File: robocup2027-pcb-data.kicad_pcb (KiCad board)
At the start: 2 copper layers, 36 parts, among them M5 Motor_Servo, M6 Motor_Servo, Q1 BPW40, Q2 BPW40, U1 ESP32-DEVKITC-32E

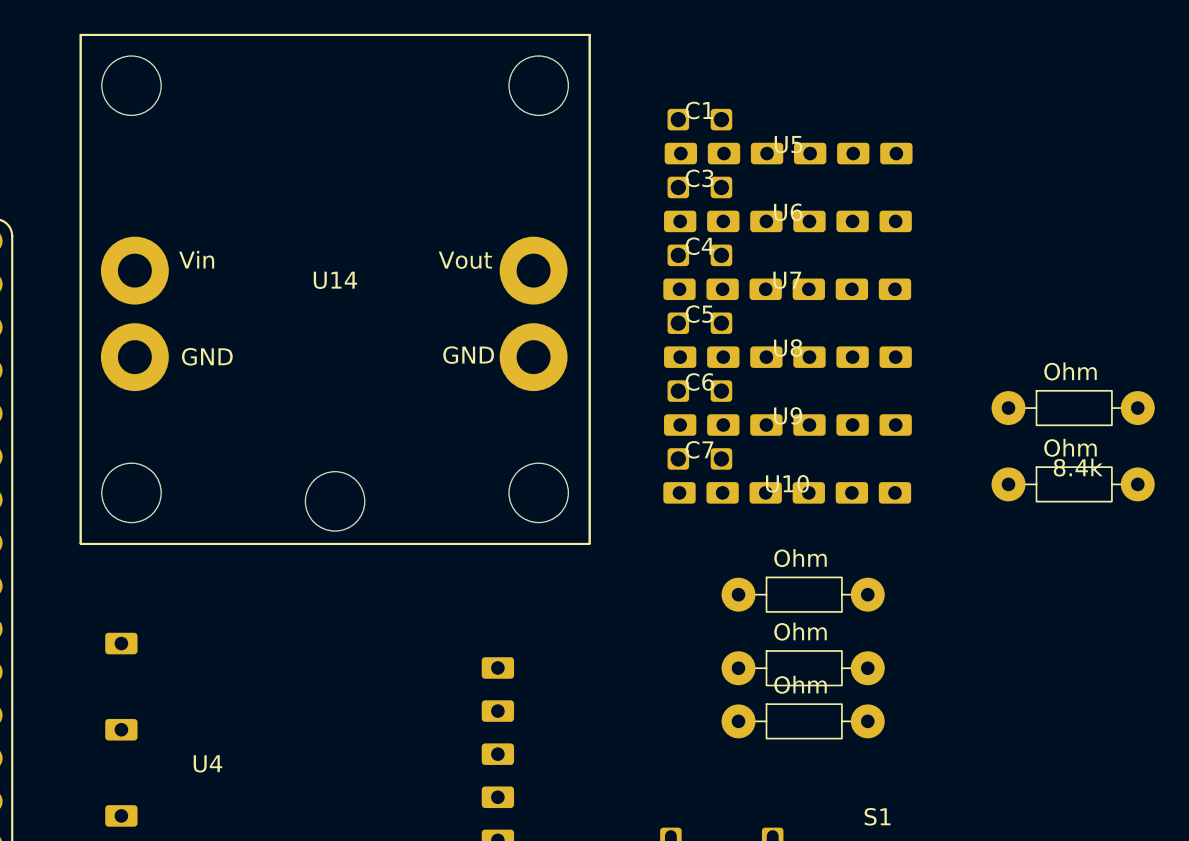
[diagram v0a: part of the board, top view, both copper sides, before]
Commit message: fixed footprint
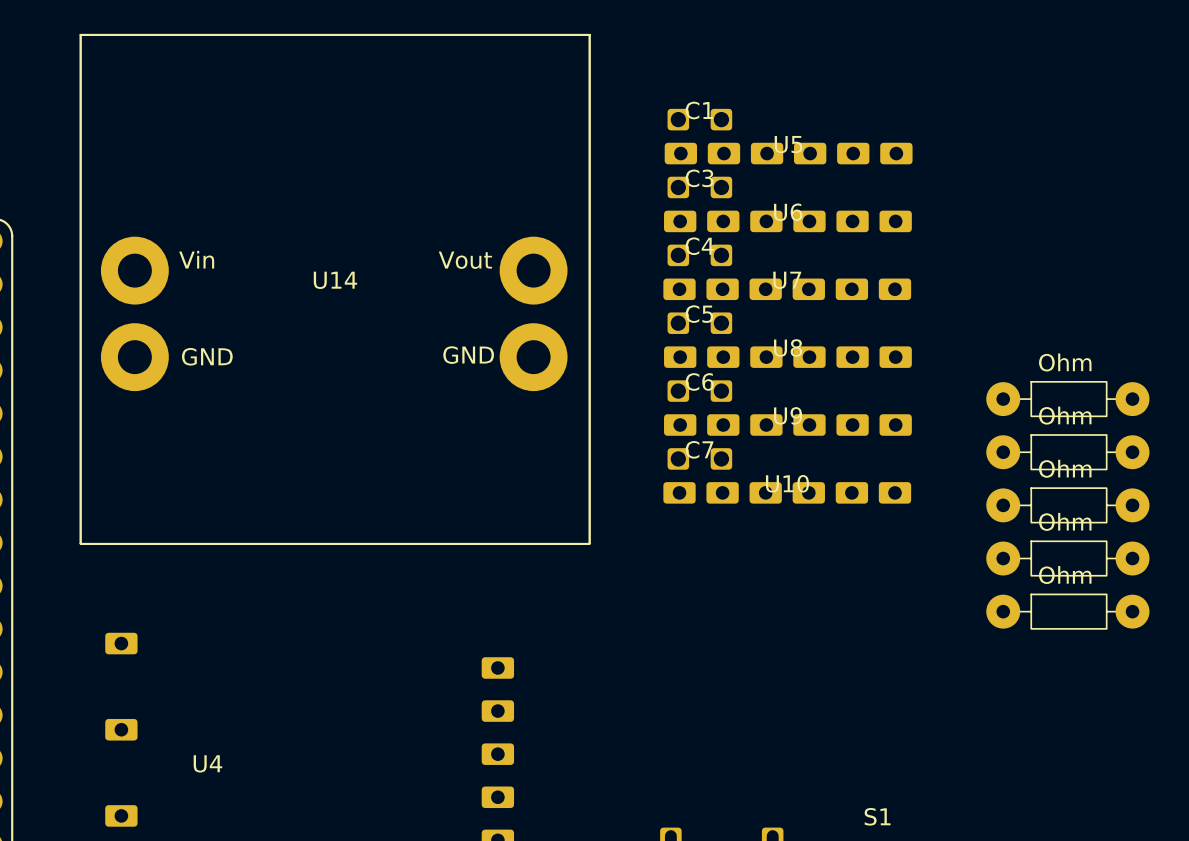
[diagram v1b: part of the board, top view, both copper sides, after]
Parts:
- moved R4 16.9 mm to (184.2, 69.4)
- moved R5 16.9 mm to (184.2, 72.5)
- moved R3 16.5 mm to (184.2, 66.2)
- moved R2 1.92 mm to (184.2, 63.1)
- moved R1 0.61 mm to (184.2, 60.0)

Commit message: update
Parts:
- C2, C8: footprint robo:5.08mm_capacitor_1 -> robo:capacitor
- Q1, Q2: footprint LED_THT:LED_D5.0mm_Clear -> robo:2.54mm_capacitor
- U11: footprint robo:M78AR033 -> robo:DCDC-M78AR033-0.5
- moved D2 29.7 mm to (104.4, 122.2)
- moved D1 29.1 mm to (105.2, 115.9)
- moved C8 27.8 mm to (123.1, 115.4)
- moved U11 25.6 mm to (124.5, 125.3)
- moved Q1 17.0 mm to (98.2, 114.9)
- moved Q2 17.0 mm to (98.4, 123.9)
- moved C2 2.43 mm to (151.4, 116.3)

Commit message: placed stuff
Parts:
- added C9: 0.1uF, robo:2.54mm_capacitor, F.Cu at (54.2, 72.5)
- added M1: ~, robo:sts3032, F.Cu at (68.5, 63.9)
- added M2: ~, robo:sts3032, F.Cu at (68.5, 66.2)
- added M3: ~, robo:sts3032, F.Cu at (68.5, 68.4)
- added M4: ~, robo:sts3032, F.Cu at (68.5, 70.7)
- added M7: ~, robo:sts3032, F.Cu at (68.5, 73.0)
- added M8: ~, robo:sts3032, F.Cu at (68.5, 75.2)
- added M9: ~, robo:sts3032, F.Cu at (68.5, 77.5)
- added U13: ~, robo:fe-urt-2, F.Cu at (58.4, 61.6)
- added U15: ~, robo:VL53L1X-ToF, F.Cu at (59.6, 59.3)
- added U16: ~, robo:DCDC-M78AR033-0.5, F.Cu at (58.1, 65.3)
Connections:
- U1 pad J3_11: unconnected-(U1-IO17-PadJ3_11) -> FE-URT-2-TXD
- U1 pad J3_12: unconnected-(U1-IO16-PadJ3_12) -> FE-URT-2-RXD

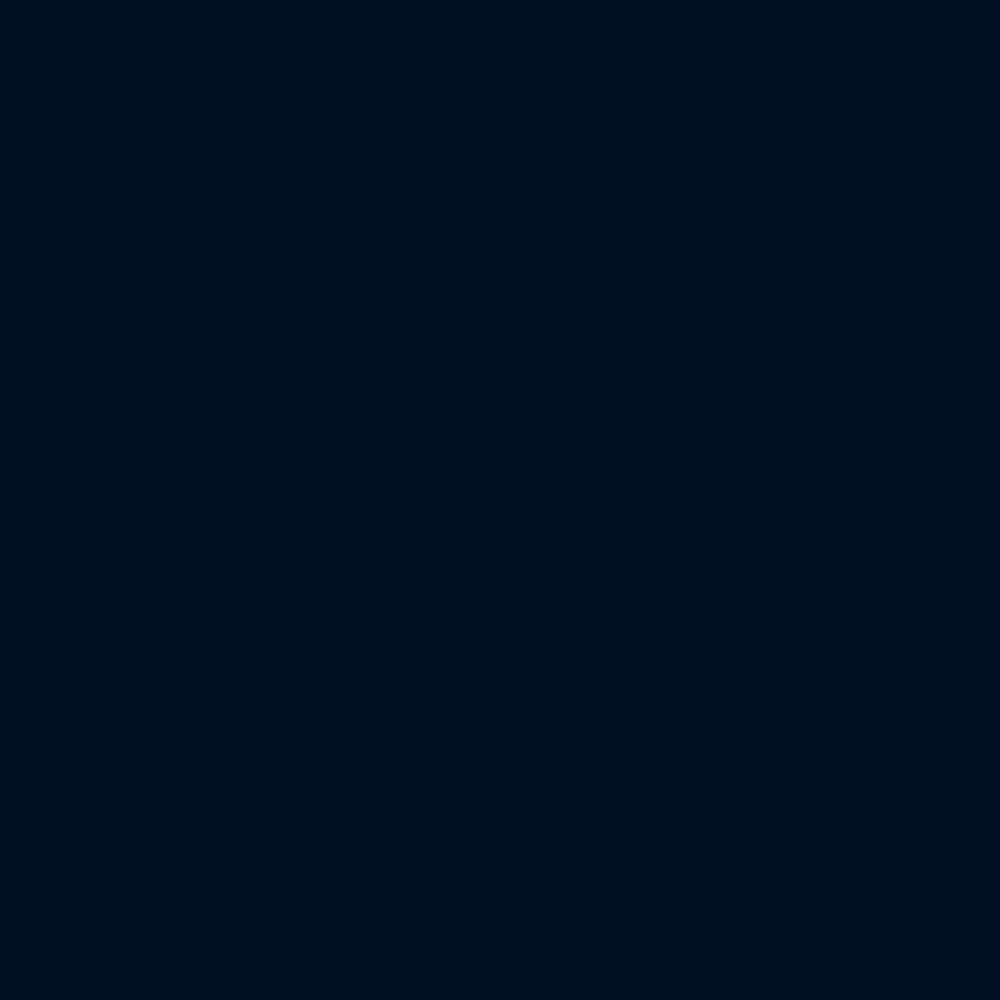
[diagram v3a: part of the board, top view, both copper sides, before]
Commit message: assigned footprints and added them to pcb
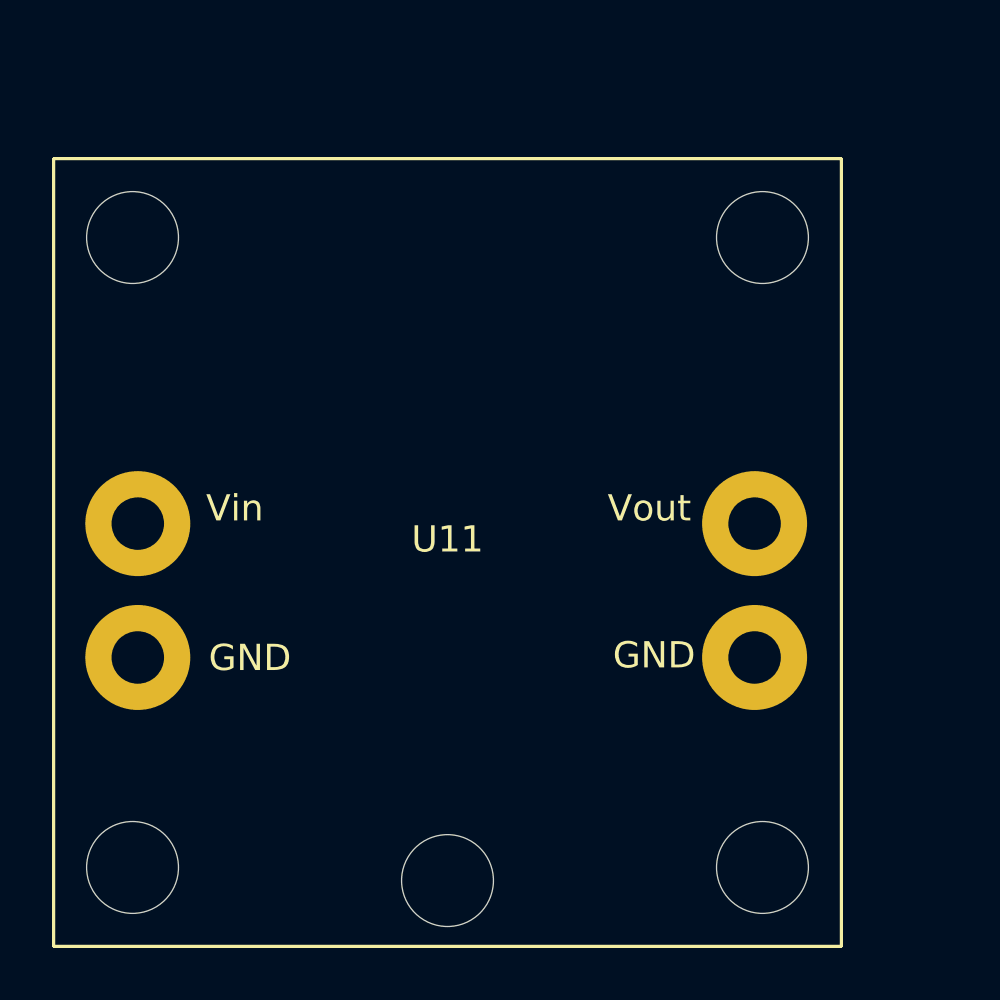
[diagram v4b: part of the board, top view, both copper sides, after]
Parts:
- added U11: ~, robo:DCDC-LTC3111, F.Cu at (57.0, 121.5)
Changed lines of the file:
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@@
+		(embedded_fonts no)
+	)
+	(footprint "robo:DCDC-LTC3111"
+		(layer "F.Cu")
+		(at 57 121.5)
+		(property "Reference" "U11"
+			(at 0 -0.5 0)
+			(unlocked yes)
+			(layer "F.SilkS")
+			(effects
+				(font
+					(size 1 1)
+					(thickness 0.1)
+				)
+			)
+		)
+		(property "Value" "~"
+			(at 0 1 0)
+			(unlocked yes)
+			(layer "F.Fab")
+			(effects
+				(font
+					(size 1 1)
+					(thickness 0.15)
+				)
+			)
+		)
+		(property "Datasheet" ""
+			(at 0 0 0)
+			(unlocked yes)
+			(layer "F.Fab")
+			(hide yes)
+			(effects
+				(font
+					(size 1 1)
+					(thickness 0.15)
+				)
+			)
+		)
+		(property "Description" ""
+			(at 0 0 0)
+			(unlocked yes)
+			(layer "F.Fab")
+			(hide yes)
+			(effects
+				(font
+					(size 1 1)
+					(thickness 0.15)
+				)
+			)
+		)
+		(sheetname "/")
+		(sheetfile "robocup2027-pcb-data.kicad_sch")
+		(attr through_hole)
+		(fp_rect
+			(start -15 -15)
+			(end -15 15)
+			(stroke
+				(width 0.1)
+				(type default)
+			)
+			(fill no)
+			(layer "F.SilkS")
+		)
+		(fp_rect
+			(start -15 -15)
+			(end 15 -15)
+			(stroke
+				(width 0.1)
+				(type default)
+			)
+			(fill no)
+			(layer "F.SilkS")
+		)
+		(fp_rect
+			(start -15 15)
+			(end 15 15)
+			(stroke
+				(width 0.1)
+				(type default)
+			)
+			(fill no)
+			(layer "F.SilkS")
+		)
+		(fp_rect
+			(start 15 -15)
+			(end 15 15)
+			(stroke
+				(width 0.1)
+				(type default)
+			)
+			(fill no)
+			(layer "F.SilkS")
+		)
+		(fp_text user "Vin"
+			(at -9.2 -1.1 0)
+			(unlocked yes)
+			(layer "F.SilkS")
+			(effects
+				(font
+					(size 1 1)
+					(thickness 0.1)
+				)
+				(justify left bottom)
+			)
+		)
+		(fp_text user "GND"
+			(at -9.1 4.6 0)
+			(unlocked yes)
+			(layer "F.SilkS")
+			(effects
+				(font
+					(size 1 1)
+					(thickness 0.1)
+				)
+				(justify left bottom)
+			)
+		)
+		(fp_text user "Vout"
+			(at 6.1 -1.1 0)
+			(unlocked yes)
+			(layer "F.SilkS")
+			(effects
+				(font
+					(size 1 1)
+					(thickness 0.1)
+				)
+				(justify left bottom)
+			)
+		)
+		(fp_text user "GND"
+			(at 6.3 4.5 0)
+			(unlocked yes)
+			(layer "F.SilkS")
+			(effects
+				(font
+					(size 1 1)
+					(thickness 0.1)
+				)
+				(justify left bottom)
+			)
+		)
+		(fp_text user "${REFERENCE}"
+			(at 0 2.5 0)
+			(unlocked yes)
+			(layer "F.Fab")
+			(effects
+				(font
+					(size 1 1)
+					(thickness 0.15)
+				)
+			)
+		)
+		(pad "" thru_hole circle
+			(at -12 -12)
+			(size 2 2)
+			(drill 3.5)
+			(layers "*.Mask")
+			(remove_unused_layers no)
+		)
+		(pad "" thru_hole circle
+			(at -12 12)
+			(size 2 2)
+			(drill 3.5)
+			(layers "*.Mask")
+			(remove_unused_layers no)
+		)
+		(pad "" thru_hole circle
+			(at 0 12.5)
+			(size 2 2)
+			(drill 3.5)
+			(layers "*.Mask")
+			(remove_unused_layers no)
+		)
+		(pad "" thru_hole circle
+			(at 12 -12)
+			(size 2 2)
+			(drill 3.5)
+			(layers "*.Mask")
+			(remove_unused_layers no)
+		)
+		(pad "" thru_hole circle
+			(at 12 12)
+			(size 2 2)
+			(drill 3.5)
+			(layers "*.Mask")
+			(remove_unused_layers no)
+		)
+		(pad "1" thru_hole circle
+			(at -11.8 -1.1)
+			(size 4 4)
+			(drill 2)
+			(layers "*.Cu" "*.Mask")
+			(remove_unused_layers no)
+			(net 14 "LiPo+")
+			(pinfunction "Vin")
+			(pintype "power_in")
+		)
+		(pad "2" thru_hole circle
+			(at -11.8 4)
+			(size 4 4)
+			(drill 2)
+			(layers "*.Cu" "*.Mask")
+			(remove_unused_layers no)
+			(net 2 "GND")
+			(pinfunction "GND")
+			(pintype "power_in")
+		)
+		(pad "3" thru_hole circle
+			(at 11.7 -1.1)
+			(size 4 4)
+			(drill 2)
+			(layers "*.Cu" "*.Mask")
+			(remove_unused_layers no)
+			(net 3 "+6V")
+			(pinfunction "Vout")
+			(pintype "power_in")
+		)
+		(pad "4" thru_hole circle
+			(at 11.7 4)
+			(size 4 4)
+			(drill 2)
+			(layers "*.Cu" "*.Mask")
+			(remove_unused_layers no)
+			(net 2 "GND")
+			(pinfunction "GND")
+			(pintype "power_in")
+		)
 		(embedded_fonts no)
 	)

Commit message: done with the placing
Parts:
- removed the U11 at (124.5, 125.3)
- removed the U11 at (57.0, 121.5)
- removed U14: ~, robo:DCDC-LTC3111
- added U11: ~, robo:DCDC-LTC3111, F.Cu at (154.5, 76.0)
- moved U16 105.3 mm to (137.8, 134.1)
- moved U13 96.8 mm to (106.1, 145.9)
- moved C1 89.4 mm to (96.8, 104.0)
- moved C3 88.2 mm to (96.8, 106.3)
- moved C4 87.1 mm to (96.8, 108.6)
- moved R4 87.0 mm to (97.3, 65.5), turned to -90 degrees
- moved C5 85.9 mm to (96.8, 110.8)
- moved C6 84.8 mm to (96.8, 113.1)
- moved U5 84.3 mm to (107.3, 104.2)
- moved C7 83.7 mm to (96.8, 115.4)
- moved U6 83.0 mm to (107.3, 106.5)
- moved R3 83.0 mm to (101.3, 70.0), turned to -90 degrees
- moved U7 81.8 mm to (107.3, 108.7)
- moved U8 80.7 mm to (107.3, 111.0)
- moved U9 79.6 mm to (107.3, 113.3)
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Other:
- board outline added: 83 x 117 mm
- copper layers 2 -> 6
